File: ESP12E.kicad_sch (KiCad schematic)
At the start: 37 parts, among them J1 Conn_01x06_Pin, J2 Conn_01x06_Pin, J3 UART, J5 12v PWR, U1 ESP-12E, U2 LM7805_TO220, U3 AMS1117-3.3, U4 HX710(A/B), U5 MPS-2108, U6 MPS-2108, U7 HX710(A/B)

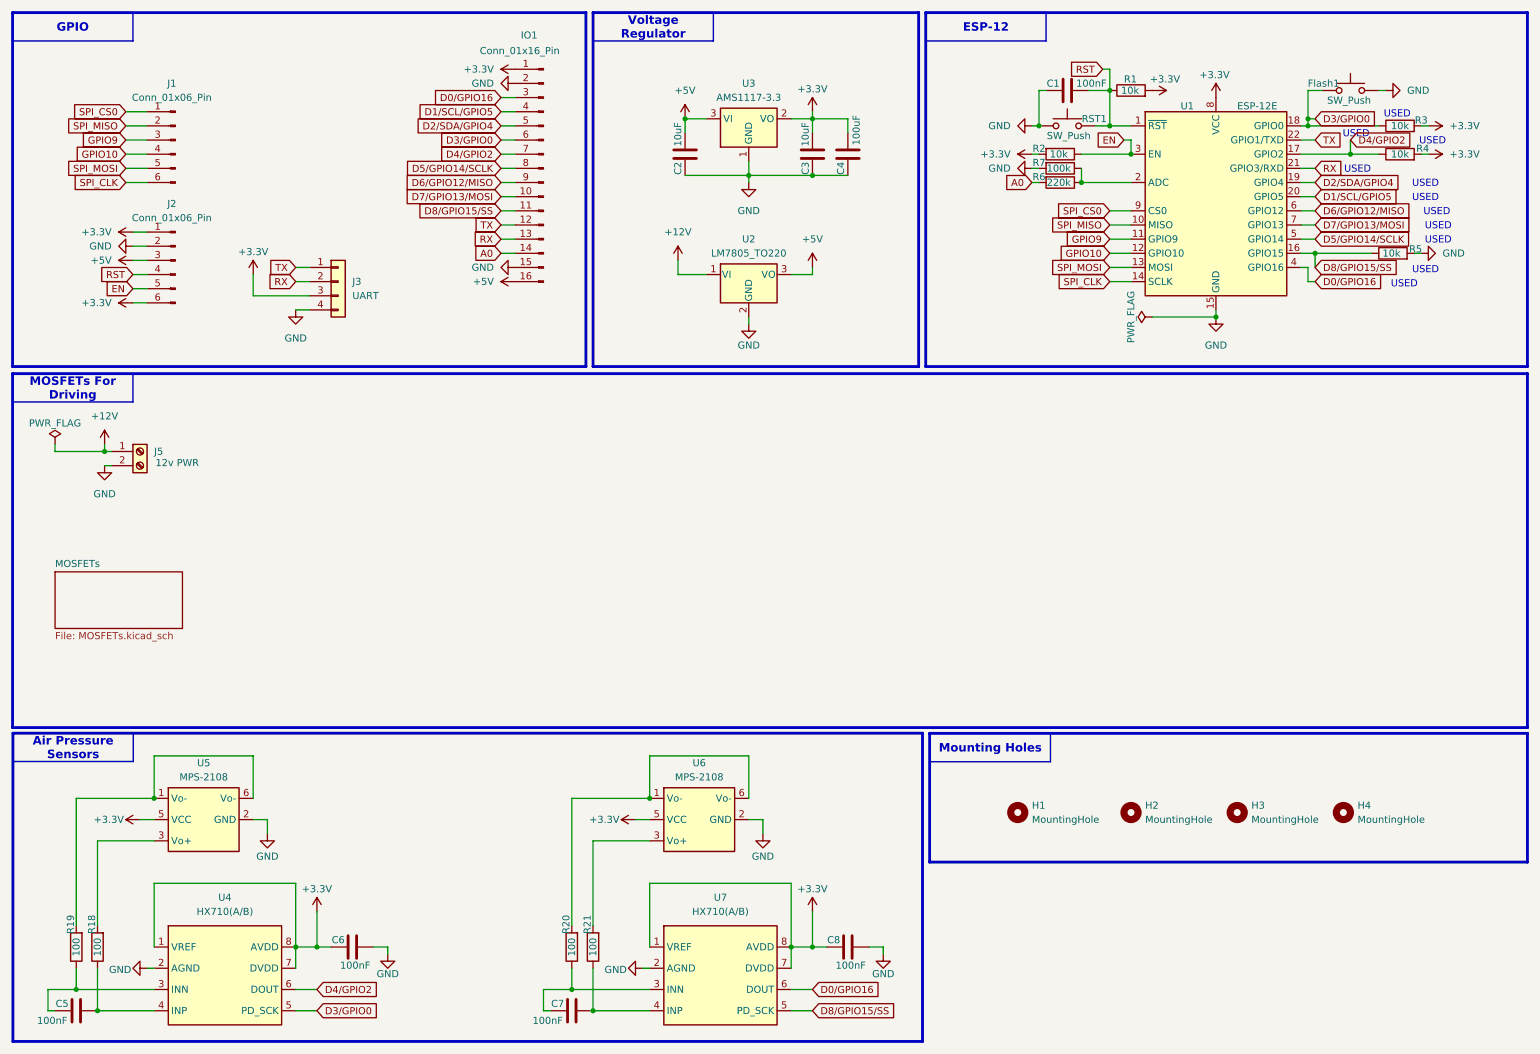
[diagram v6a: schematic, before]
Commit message: Feat: adding Buck converter + making BOM files HTML with LINKs of stores + small edits + adding polarity protection.
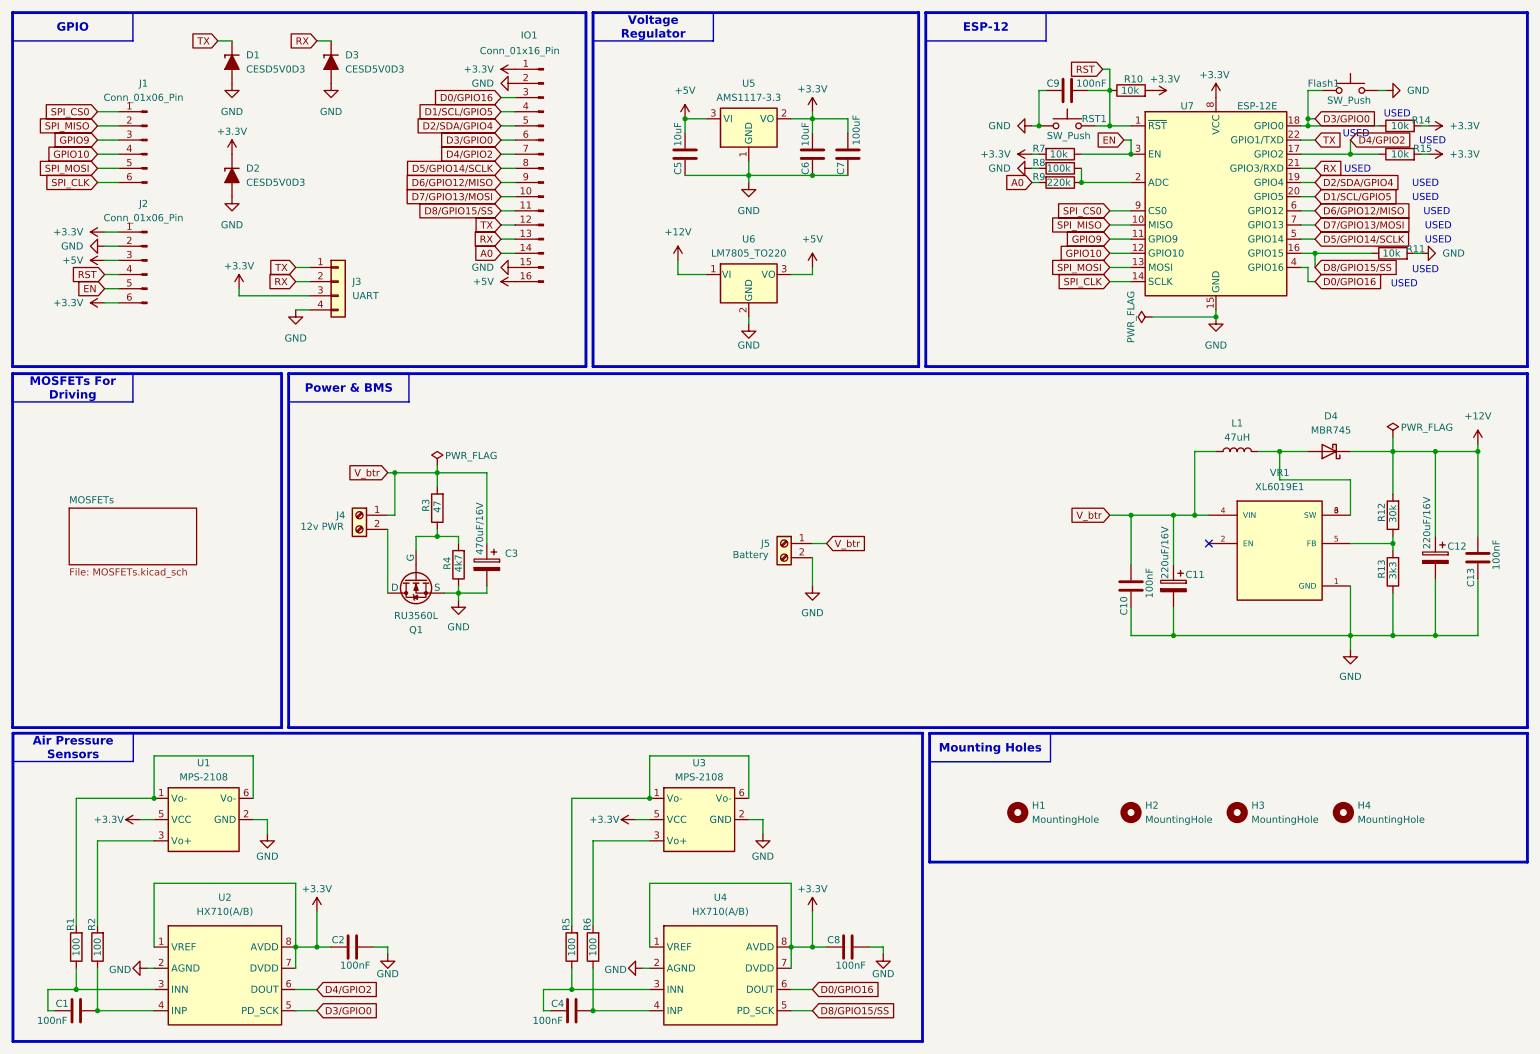
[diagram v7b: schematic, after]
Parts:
- added C10, C13: 100nF, Capacitor_THT:C_Disc_D3.0mm_W2.0mm_P2.50mm, symbol Device:C
- added C11, C12: 220uF/16V, Capacitor_THT:CP_Radial_D10.0mm_P3.80mm, symbol Device:C_Polarized
- added C3: 470uF/16V, Capacitor_THT:CP_Radial_D10.0mm_P3.80mm, symbol Device:C_Polarized
- added D1, D2, D3: CESD5V0D3, Diode_SMD:D_SOD-323_HandSoldering, symbol Diode:D_TVS_Unidirectional_Generic
- added D4: MBR745, Package_TO_SOT_THT:TO-220-2_Vertical, symbol Diode:MBR745
- added J5: Battery, TerminalBlock_RND:TerminalBlock_RND_205-00276_1x02_P5.00mm_Vertical, symbol Connector:Screw_Terminal_01x02
- added L1: 47uH, Inductor_THT:L_Toroid_Vertical_L14.7mm_W8.6mm_P5.58mm_Pulse_KM-1, symbol Device:L
- added Q1: RU3560L, Package_TO_SOT_SMD:TO-252-2, symbol Simulation_SPICE:NMOS
- added R12: 30k, Resistor_SMD:R_1206_3216Metric_Pad1.30x1.75mm_HandSolder, symbol Device:R
- added R13: 3k3, Resistor_SMD:R_1206_3216Metric_Pad1.30x1.75mm_HandSolder, symbol Device:R
- added R3: 47, Resistor_SMD:R_1206_3216Metric_Pad1.30x1.75mm_HandSolder, symbol Device:R
- added R4: 4k7, Resistor_SMD:R_1206_3216Metric_Pad1.30x1.75mm_HandSolder, symbol Device:R
- added VR1: XL6019E1, Converter_DCDC:TO-263-5, symbol Converter_DCDC:XL6019E1
- C1: renamed from C5; LINK (none) -> https://makerselectronics.com/product/ceramic-capacitor-100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
- C2: renamed from C6; LINK (none) -> https://makerselectronics.com/product/ceramic-capacitor-100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
- C4: renamed from C7; LINK (none) -> https://makerselectronics.com/product/ceramic-capacitor-100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
- C5: renamed from C2; LINK (none) -> https://makerselectronics.com/product/capacitor-10uf-50v
- C6: renamed from C3; LINK (none) -> https://makerselectronics.com/product/capacitor-10uf-50v
- C7: renamed from C4; LINK (none) -> https://makerselectronics.com/product/capacitor-100uf-25v
- C8: LINK (none) -> https://makerselectronics.com/product/ceramic-capacitor-100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
- C9: renamed from C1; LINK (none) -> https://makerselectronics.com/product/ceramic-capacitor-100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
- Flash1, RST1: footprint Button_Switch_SMD:SW_SPST_B3U-1000P -> Button_Switch_SMD:SW_SKRPACE010; LINK (none) -> https://makerselectronics.com/product/smd-tactile-push-butt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
- IO1, J1, J2: LINK (none) -> N/A
- J3: LINK (none) -> https://makerselectronics.com/product/b4b-xh-a-jst-xh-4-pin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
- J4: renamed from J5; LINK (none) -> https://makerselectronics.com/product/terminal-block-kf2edg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
- R1: renamed from R19; LINK (none) -> https://makerselectronics.com/product/chip-resistor-smd-100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
- R10: renamed from R1; LINK (none) -> https://makerselectronics.com/product/chip-resistor-smd-10k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
- R11: renamed from R5; LINK (none) -> https://makerselectronics.com/product/chip-resistor-smd-10k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
- R14: renamed from R3; LINK (none) -> https://makerselectronics.com/product/chip-resistor-smd-10k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
- R15: renamed from R4; LINK (none) -> https://makerselectronics.com/product/chip-resistor-smd-10k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
- R2: renamed from R18; LINK (none) -> https://makerselectronics.com/product/chip-resistor-smd-100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
- R5: renamed from R20; LINK (none) -> https://makerselectronics.com/product/chip-resistor-smd-100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
- R6: renamed from R21; LINK (none) -> https://makerselectronics.com/product/chip-resistor-smd-100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
- R7: renamed from R2; LINK (none) -> https://makerselectronics.com/product/chip-resistor-smd-10k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
- R8: renamed from R7; LINK (none) -> https://makerselectronics.com/product/chip-resistor-smd-100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
- R9: renamed from R6; LINK (none) -> https://makerselectronics.com/product/chip-resistor-smd-220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
- U1: renamed from U5; LINK (none) -> https://www.ram-e-shop.com/shop/sen-pressure-mps2108-mps-21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
- U2: renamed from U4; LINK (none) -> https://free-electronic.com/product/hx710b
- U3: renamed from U6; LINK (none) -> https://www.ram-e-shop.com/shop/sen-pressure-mps2108-mps-21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
- U4: renamed from U7; LINK (none) -> https://free-electronic.com/product/hx710b
- U5: renamed from U3; LINK (none) -> https://makerselectronics.com/product/ams1117-3-3v-smd-fixe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
- U6: renamed from U2; LINK (none) -> https://makerselectronics.com/product/lm7805-voltage-regula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
- U7: renamed from U1; LINK (none) -> https://free-electronic.com/product/wifi-serial-module-esp8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
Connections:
- net +12V: now also C12.1, C13.2, D4.1 (K), R12.2; no longer J4.1 (Pin_1)
- net +3.3V: now also D2.1 (K)
- net GND: now also C10.1, C11.2, C12.2, C13.1, C3.2, D1.2 (A), D2.2 (A), D3.2 (A), J5.2 (Pin_2), Q1.3 (S), R13.1, R4.1, VR1.1 (GND); no longer J4.2 (Pin_2)
- net RX: now also D3.1 (K)
- net TX: now also D1.1 (K)
- new net: Q1.1 (G), R3.1, R4.2
- new net: R12.1, R13.2, VR1.5 (FB)
- new net: J4.2 (Pin_2), Q1.2 (D)
- new net: D4.2 (A), L1.2, VR1.3 (SW), VR1.6 (SW)
- new net V_btr: C10.2, C11.1, C3.1, J4.1 (Pin_1), J5.1 (Pin_1), L1.1, R3.2, VR1.4 (VIN)
- no-connect marks 0 -> 1
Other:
- moved on the sheet: J1, J2, J4

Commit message: Feat: the board now has a circuit that manage       the switch between Battery and Adaptor Power.
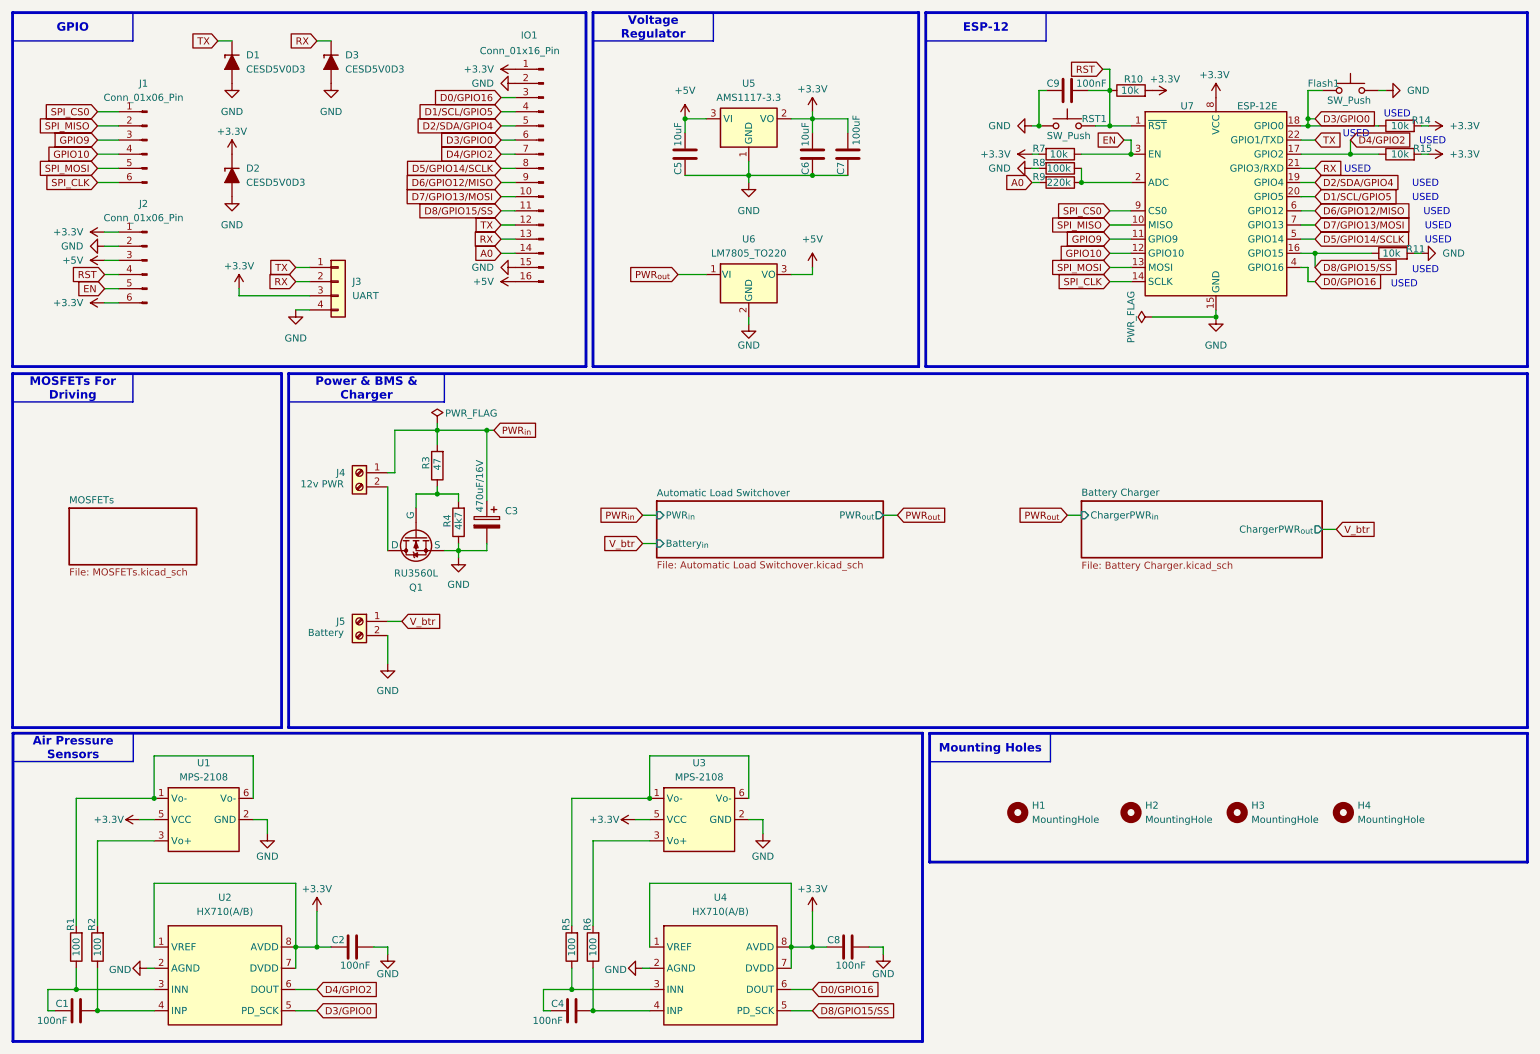
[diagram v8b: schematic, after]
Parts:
- removed C10, C13: 100nF, Capacitor_THT:C_Disc_D3.0mm_W2.0mm_P2.50mm, symbol Device:C
- removed C11, C12: 220uF/16V, Capacitor_THT:CP_Radial_D10.0mm_P3.80mm, symbol Device:C_Polarized
- removed D4: MBR745, Package_TO_SOT_THT:TO-220-2_Vertical, symbol Diode:MBR745
- removed L1: 47uH, Inductor_THT:L_Toroid_Vertical_L14.7mm_W8.6mm_P5.58mm_Pulse_KM-1, symbol Device:L
- removed R12: 30k, Resistor_SMD:R_1206_3216Metric_Pad1.30x1.75mm_HandSolder, symbol Device:R
- removed R13: 3k3, Resistor_SMD:R_1206_3216Metric_Pad1.30x1.75mm_HandSolder, symbol Device:R
- removed VR1: XL6019E1, Converter_DCDC:TO-263-5, symbol Converter_DCDC:XL6019E1
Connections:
- net V_btr: no longer C3.1, J4.1 (Pin_1), R3.2
- net +12V renamed PWR_{out}
- new net PWR_{in}: C3.1, J4.1 (Pin_1), R3.2
- no-connect marks 1 -> 0
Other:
- added sheet Automatic Load Switchover (Automatic Load Switchover.kicad_sch)
- added sheet Battery Charger (Battery Charger.kicad_sch)
- moved on the sheet: C3, J4, J5, Q1, R3, R4
